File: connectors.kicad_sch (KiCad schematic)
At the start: 34 parts, among them J301 CONN_SMA_VERT, J302 CONN2, J303 CONN_SMA_VERT, J304 CONN3, J305 CONN_SMA_VERT, J306 CONN3, J307 CONN2, J308 CONN_SMA_VERT, J309 CONN8, Q301 BSS138

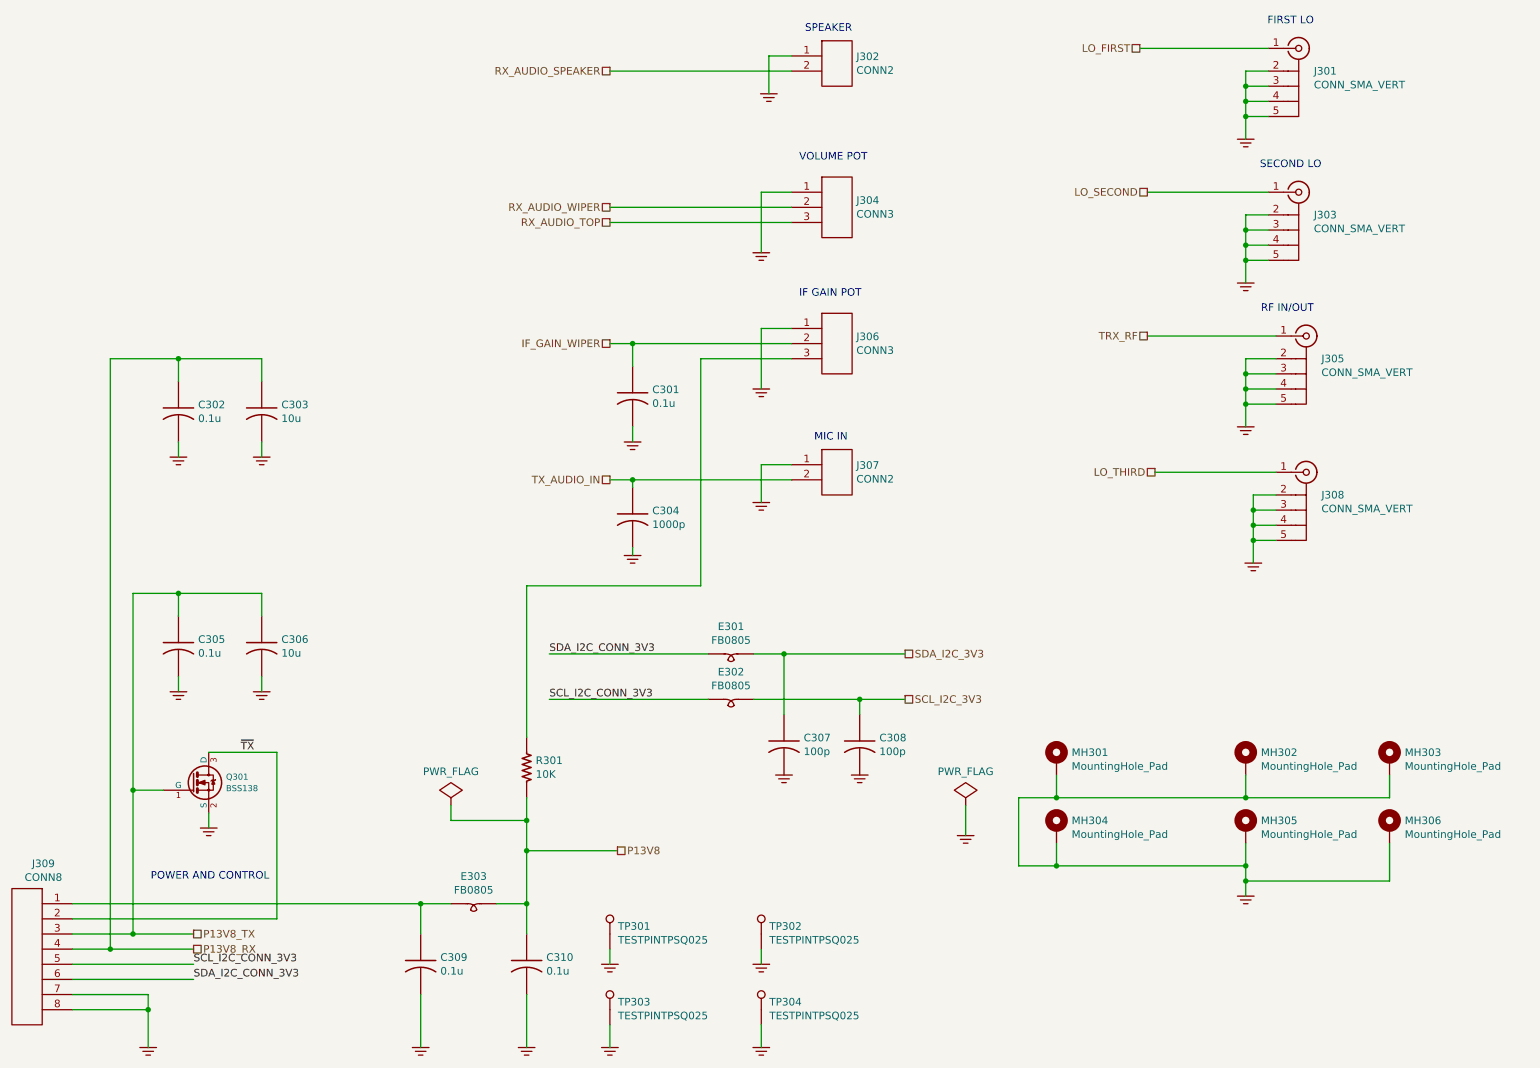
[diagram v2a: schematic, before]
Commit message: trx_mobo_concept_2_B. Change design to use a dedicated 8V supply for the 2SC3357 parts. Add S-Meter connector. Change mic connector to 3 pins and add 8V sopower supply to pin 3.
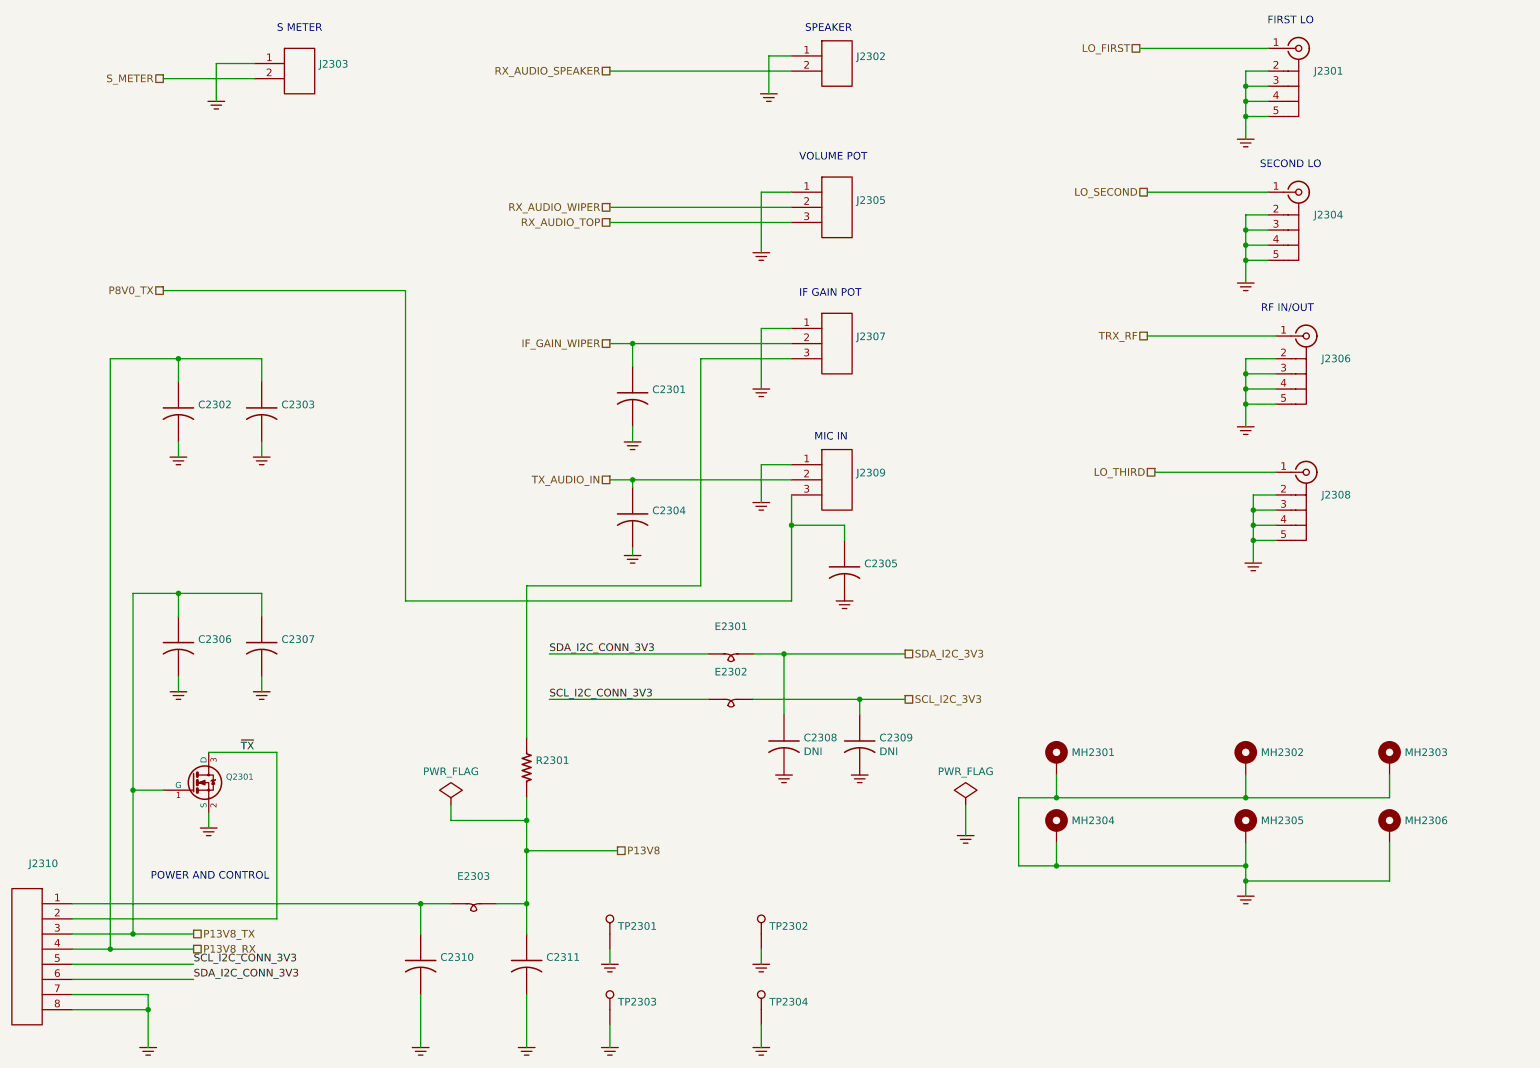
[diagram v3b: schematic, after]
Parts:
- removed J307: CONN2, mods:JST_B2B_XH_A, symbol custom:CONN2
- added C2305: (no value), symbol custom:C_US_0805_0.1UF_X7R_10%_50V_HS
- added J2303: (no value), symbol custom:CONN2
- added J2309: (no value), symbol custom:CONN3
- C2301: renamed from C301; value 0.1u -> (none); footprint Capacitor_SMD:C_0805_2012Metric_Pad1.15x1.40mm_HandSolder -> (none)
- C2302: renamed from C302; value 0.1u -> (none); footprint Capacitor_SMD:C_0805_2012Metric_Pad1.15x1.40mm_HandSolder -> (none)
- C2303: renamed from C303; value 10u -> (none); footprint Capacitor_SMD:C_0805_2012Metric_Pad1.15x1.40mm_HandSolder -> (none)
- C2304: renamed from C304; value 1000p -> (none); footprint Capacitor_SMD:C_0805_2012Metric_Pad1.15x1.40mm_HandSolder -> (none); PartNumber 800239-103 -> 800239-102
- C2306: renamed from C305; value 0.1u -> (none); footprint Capacitor_SMD:C_0805_2012Metric_Pad1.15x1.40mm_HandSolder -> (none)
- C2307: renamed from C306; value 10u -> (none); footprint Capacitor_SMD:C_0805_2012Metric_Pad1.15x1.40mm_HandSolder -> (none)
- C2308: renamed from C307; value 100p -> DNI; footprint Capacitor_SMD:C_0805_2012Metric_Pad1.15x1.40mm_HandSolder -> (none)
- C2309: renamed from C308; value 100p -> DNI; footprint Capacitor_SMD:C_0805_2012Metric_Pad1.15x1.40mm_HandSolder -> (none)
- C2310: renamed from C309; value 0.1u -> (none); footprint Capacitor_SMD:C_0805_2012Metric_Pad1.15x1.40mm_HandSolder -> (none)
- C2311: renamed from C310; value 0.1u -> (none); footprint Capacitor_SMD:C_0805_2012Metric_Pad1.15x1.40mm_HandSolder -> (none)
- E2301: renamed from E301; value FB0805 -> (none); footprint Inductor_SMD:L_0805_2012Metric_Pad1.15x1.40mm_HandSolder -> (none)
- E2302: renamed from E302; value FB0805 -> (none); footprint Inductor_SMD:L_0805_2012Metric_Pad1.15x1.40mm_HandSolder -> (none)
- E2303: renamed from E303; value FB0805 -> (none); footprint Inductor_SMD:L_0805_2012Metric_Pad1.15x1.40mm_HandSolder -> (none)
- J2301: renamed from J301; value CONN_SMA_VERT -> (none); footprint mods:SMA_Kinghelm_KHSMA-KE8-G_Vertical -> (none)
- J2302: renamed from J302; value CONN2 -> (none); footprint mods:JST_B2B_XH_A -> (none)
- J2304: renamed from J303; value CONN_SMA_VERT -> (none); footprint mods:SMA_Kinghelm_KHSMA-KE8-G_Vertical -> (none)
- J2305: renamed from J304; value CONN3 -> (none); footprint mods:JST_B3B_XH_A -> (none)
- J2306: renamed from J305; value CONN_SMA_VERT -> (none); footprint mods:SMA_Kinghelm_KHSMA-KE8-G_Vertical -> (none)
- J2307: renamed from J306; value CONN3 -> (none); footprint mods:JST_B3B_XH_A -> (none)
- J2308: renamed from J308; value CONN_SMA_VERT -> (none); footprint mods:SMA_Kinghelm_KHSMA-KE8-G_Vertical -> (none)
- J2310: renamed from J309; value CONN8 -> (none); footprint mods:JST_B8B_XH_A -> (none)
- MH2301: renamed from MH301; value MountingHole_Pad -> (none); footprint MountingHole:MountingHole_3.5mm_Pad_Via -> (none)
- MH2302: renamed from MH302; value MountingHole_Pad -> (none); footprint MountingHole:MountingHole_3.5mm_Pad_Via -> (none)
- MH2303: renamed from MH303; value MountingHole_Pad -> (none); footprint MountingHole:MountingHole_3.5mm_Pad_Via -> (none)
- MH2304: renamed from MH304; value MountingHole_Pad -> (none); footprint MountingHole:MountingHole_3.5mm_Pad_Via -> (none)
- MH2305: renamed from MH305; value MountingHole_Pad -> (none); footprint MountingHole:MountingHole_3.5mm_Pad_Via -> (none)
- MH2306: renamed from MH306; value MountingHole_Pad -> (none); footprint MountingHole:MountingHole_3.5mm_Pad_Via -> (none)
- Q2301: renamed from Q301; value BSS138 -> (none); footprint mods:SOT23-3-SAR -> (none)
- R2301: renamed from R301; value 10K -> (none); footprint Resistor_SMD:R_0805_2012Metric_Pad1.15x1.40mm_HandSolder -> (none)
- TP2301: renamed from TP301; value TESTPINTPSQ025 -> (none); footprint mods:TESTPIN -> (none)
- TP2302: renamed from TP302; value TESTPINTPSQ025 -> (none); footprint mods:TESTPIN -> (none)
- TP2303: renamed from TP303; value TESTPINTPSQ025 -> (none); footprint mods:TESTPIN -> (none)
- TP2304: renamed from TP304; value TESTPINTPSQ025 -> (none); footprint mods:TESTPIN -> (none)
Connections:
- net GND: now also C2305.2, J2303.1, J2309.1
- net TX_AUDIO_IN: now also J2309.2
- new net P8V0_TX: C2305.1, J2309.3
- new net S_METER: J2303.2
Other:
- note added: "S METER"

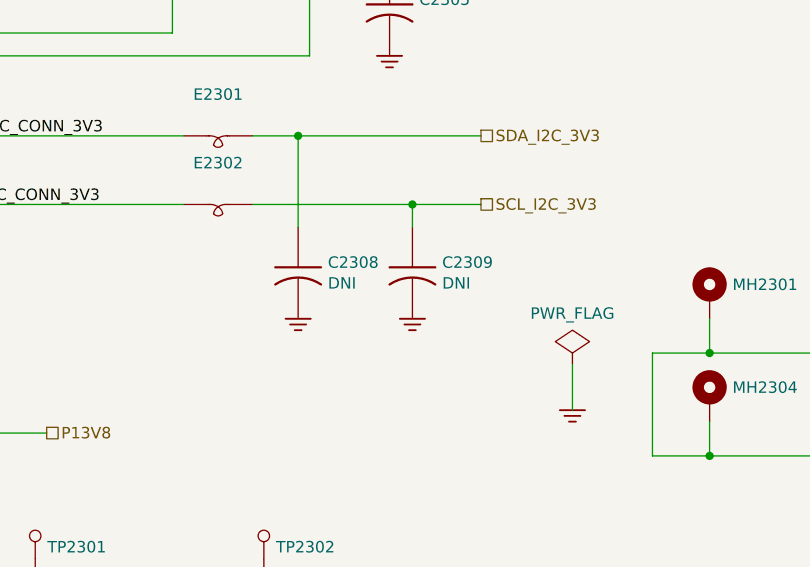
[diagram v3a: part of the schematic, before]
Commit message: Fix 12.288MHz part number in schematic, regenerate BOM's.
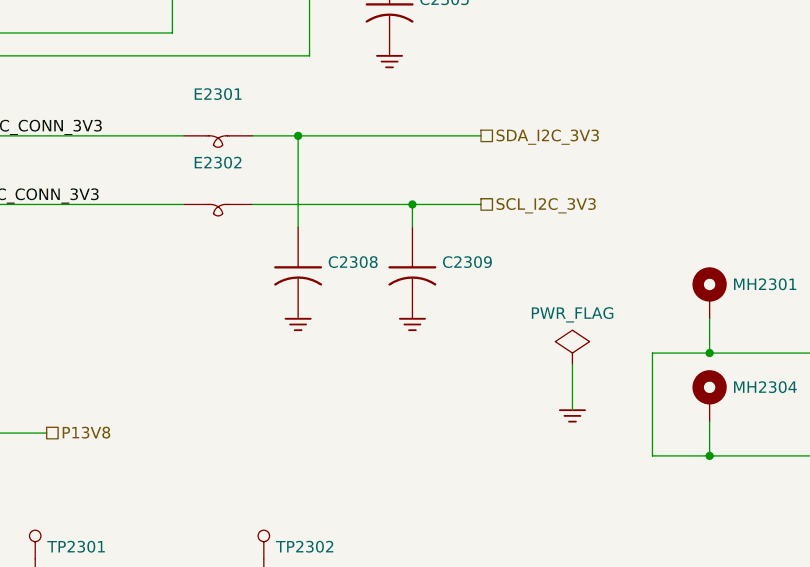
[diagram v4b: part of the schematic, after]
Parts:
- C2308, C2309: value DNI -> (none)
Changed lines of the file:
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@@
       (effects (font (size 1.27 1.27)) (justify left))
     )
-    (property "Value" "DNI" (id 1) (at 146.812 144.653 0)
+    (property "Value" "" (id 1) (at 146.812 144.653 0)
       (effects (font (size 1.27 1.27)) (justify left))
     )
@@
       (effects (font (size 1.27 1.27)) (justify left))
     )
-    (property "Value" "DNI" (id 1) (at 159.512 144.653 0)
+    (property "Value" "" (id 1) (at 159.512 144.653 0)
       (effects (font (size 1.27 1.27)) (justify left))
     )
